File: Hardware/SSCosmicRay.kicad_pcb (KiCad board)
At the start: 2 copper layers, 80 x 50 mm, 115 parts, among them J1 ICSP-PIC, J2 USB_MINI, SW1 PGM, SW2 RST, U1 MAX4477, U2 MAX4477, U3 MAX991, U4 741G08, U5 PIC32MX250F128B, U6 MAX4477, U7 MAX4477, U8 LTC3129-SOP, U9 AOZ1280, X1 8MHz

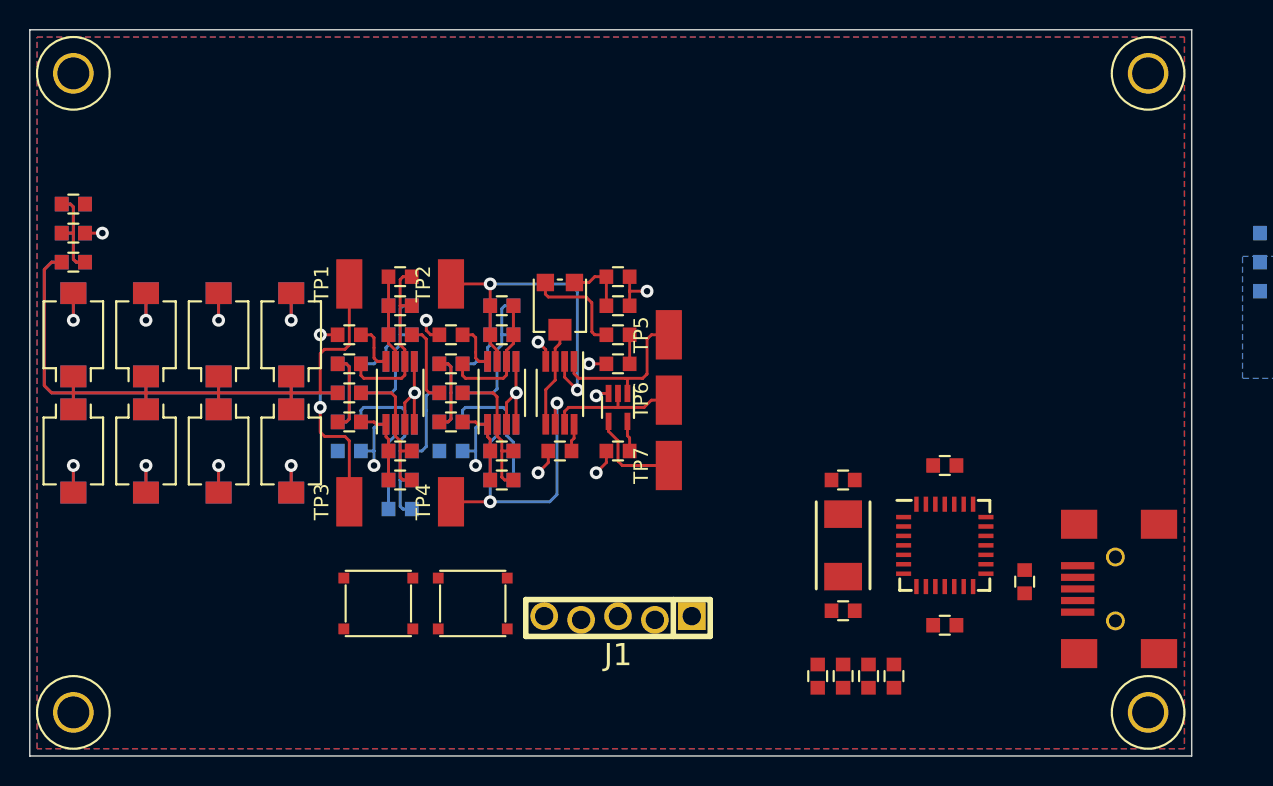
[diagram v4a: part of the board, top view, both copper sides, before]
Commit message: Switch to 44 pin PIC
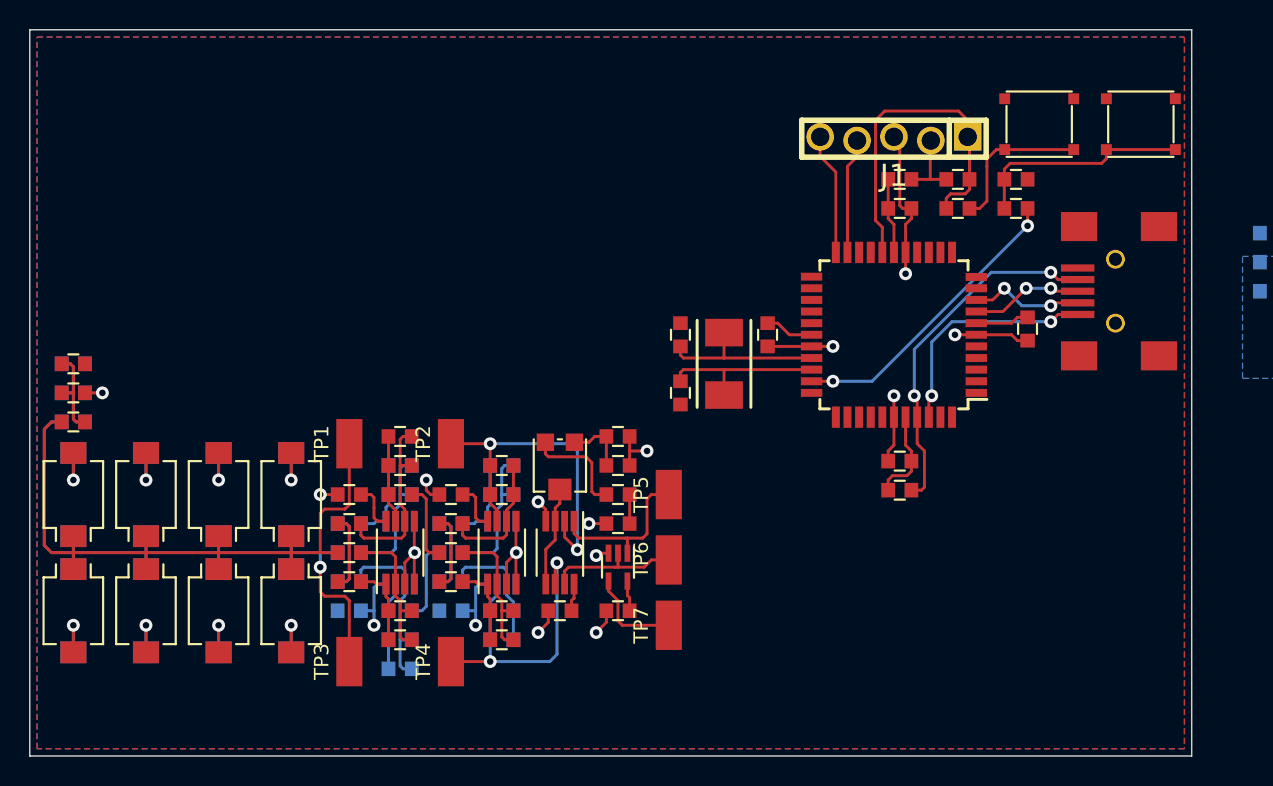
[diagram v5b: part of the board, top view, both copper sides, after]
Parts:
- removed MECH-HOLE220 (x4): VAL**, MECH-HOLE220
- added C41: 0.1uF, CAPC1608-N, F.Cu at (186.9, 65.3)
- added R31: 10k, RESC1608-N, F.Cu at (186.9, 84.7)
- added R32: 10, RESC1608-N, F.Cu at (186.9, 63.3)
- R15: value R -> 10k
- U5: value PIC32MX250F128B -> PIC32MX250F128D; footprint QFN65P600X600-28N -> QFP80P1200x1200-44N
- moved SW1 62.0 mm to (203.5, 59.5), turned to 180 degrees
- moved SW2 51.1 mm to (196.5, 59.5), turned to 180 degrees
- moved J1 38.1 mm to (186.5, 60.5)
- moved R13 36.2 mm to (194.9, 63.3), turned to 180 degrees
- moved R12 35.0 mm to (194.9, 65.3), turned to 180 degrees
- moved R14 34.5 mm to (190.9, 63.3), turned to 0 degrees
- moved R15 32.8 mm to (190.9, 65.3), turned to 0 degrees
- moved J2 20.5 mm to (207.0, 71.0)
- moved C17 18.7 mm to (171.8, 78.0), turned to 270 degrees
- moved C18 17.4 mm to (195.7, 73.6)
- moved C19 15.2 mm to (177.8, 74.0), turned to 270 degrees
- moved C16 15.0 mm to (171.8, 74.0), turned to 90 degrees
- moved X1 14.9 mm to (174.8, 76.0)
- moved U5 14.9 mm to (186.5, 74.0), turned to 180 degrees
- moved C20 11.7 mm to (186.9, 82.7), turned to 180 degrees
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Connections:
- U5 pad 1: /Processor/PGD -> (no net)
- U5 pad 11: /Processor/ID -> (no net)
- U5 pad 12: /Processor/VBus -> (no net)
- U5 pad 17: /Processor/VCap -> /Processor/VAng
- U5 pad 18: /Processor/D+ -> /Processor/MCLR
- U5 pad 19: /Processor/D- -> (no net)
- U5 pad 2: /Processor/PGC -> (no net)
- U5 pad 20: +3.3V -> (no net)
- U5 pad 21: (no net) -> /Processor/PGD
- U5 pad 22: (no net) -> /Processor/PGC
- U5 pad 23: (no net) -> /Processor/A1
- U5 pad 24: GND -> /Processor/A2
- U5 pad 25: +3.3V -> /Processor/C1
- U5 pad 26: /Processor/MCLR -> /Processor/C2
- U5 pad 27: (no net) -> /Processor/C
- U5 pad 28: (no net) -> +3.3V
- U5 pad 5: GND -> (no net)
- U5 pad 6: /Processor/OSC1 -> GND
- U5 pad 7: /Processor/OSC2 -> /Processor/VCap
- U5 pad 8: /Processor/PGM -> /Processor/D+
- U5 pad 9: (no net) -> /Processor/D-
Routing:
- net GND: track 71.5 -> 96.3 mm, vias 25 -> 29
- net /Processor/ID: track 0.00 -> 24.4 mm, vias 0 -> 2
- net /Processor/MCLR: track 0.00 -> 23.5 mm
- net /Processor/PGM: track 0.00 -> 20.5 mm, vias 0 -> 2
- net /Processor/VBus: track 0.00 -> 16.1 mm, vias 0 -> 2
- net N-0000028: track 0.00 -> 15.4 mm
- net +3.3V: track 21.5 -> 36.4 mm
- net /Processor/OSC2: track 0.00 -> 11.5 mm
- net /Processor/OSC1: track 0.00 -> 11.5 mm
- net N-0000027: track 0.00 -> 10.6 mm
- net /Processor/PGC: track 0.00 -> 8.40 mm
- net /Processor/PGD: track 0.00 -> 7.98 mm
- net /Processor/D-: track 0.00 -> 7.89 mm, vias 0 -> 2
- net /Processor/D+: track 0.00 -> 7.73 mm, vias 0 -> 2
- net /Processor/VAng: track 0.00 -> 5.20 mm
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
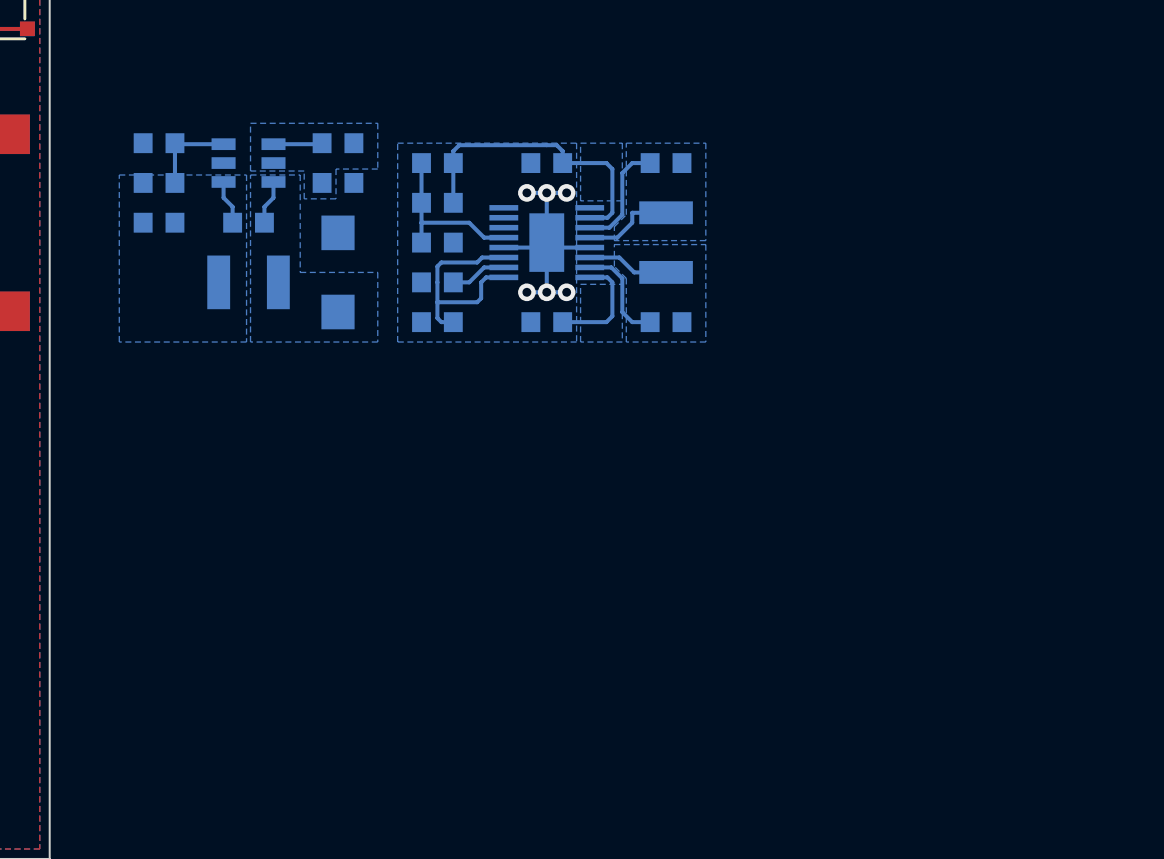
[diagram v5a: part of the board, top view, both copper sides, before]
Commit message: Change bias supply to reference layout
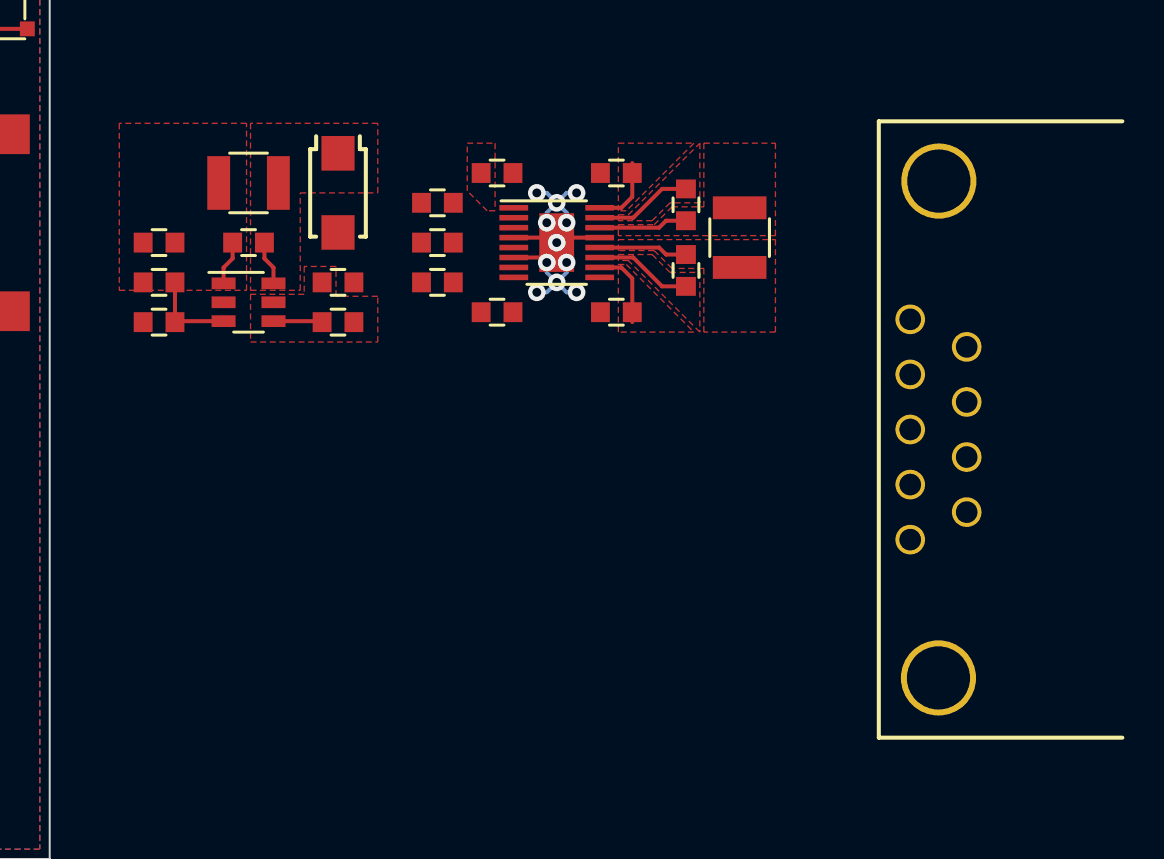
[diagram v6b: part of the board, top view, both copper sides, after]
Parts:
- added J3: CONN-9, CONN-TE-1734354, F.Cu at (261.2, 81.4)
- C32, C33, C34, C35, C36, C37, C38, C39, C40, D17, L1, L2, R25, R26, R27, R28, R29, R30, U8, U9: moved to F.Cu
- moved R27 9.00 mm to (221.5, 76.0)
- moved R29 9.00 mm to (212.5, 76.0)
- moved C34 8.28 mm to (235.5, 68.5)
- moved C36 8.28 mm to (235.5, 75.5)
- moved C35 8.08 mm to (229.5, 75.5)
- moved C37 8.08 mm to (229.5, 68.5), turned to 0 degrees
- moved U9 7.00 mm to (217.0, 75.0), turned to 270 degrees
- moved C32 5.98 mm to (239.0, 70.1), turned to 90 degrees
- moved C33 5.49 mm to (239.0, 73.4), turned to 270 degrees
- moved C40 5.00 mm to (221.5, 74.0)
- moved L2 5.00 mm to (217.0, 69.0)
- moved R28 5.00 mm to (212.5, 74.0)
- moved D17 4.00 mm to (221.5, 69.5), turned to 270 degrees
- moved R25 4.00 mm to (226.5, 74.0)
- moved R30 4.00 mm to (226.5, 70.0)
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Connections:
- C37 pad 1: N-0000082 (its old number) -> /Power/Vcc
- U5 pad 1: (no net) -> /Processor/SDA/DO
- U5 pad 44: (no net) -> /Processor/SCL/DI
- U8 pad 1: N-0000082 (its old number) -> /Power/Vcc
- U8 pad 3: N-0000082 (its old number) -> /Power/Vcc
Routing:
- net GND: track 96.3 -> 109.1 mm, vias 29 -> 34
- net N-0000082 (its old number): track 11.3 -> 0.00 mm
- net +12V: track 15.0 -> 4.07 mm
- net N-0000084: track 8.45 -> 0.00 mm
- net N-0000081: track 2.85 -> 0.00 mm
- net VCOM: track 5.57 -> 3.57 mm
- net /Power/BS2: track 5.62 -> 4.94 mm
- added copper zone on F.Cu, net +12V
- added copper zone on F.Cu, net /Power/BS1
- added copper zone on F.Cu, net /Power/BS2
- added copper zone on F.Cu, net /Power/Lx
- added copper zone on F.Cu, net /Power/SW1
- added copper zone on F.Cu, net /Power/SW2
- added copper zone on F.Cu, net /Power/Vcc
- added copper zone on F.Cu, net VCOM
- removed copper zone on B.Cu, net +12V
- removed copper zone on B.Cu, net +3.3V
- removed copper zone on B.Cu, net /Power/Lx
- removed copper zone on B.Cu, net /Power/SW1
- removed copper zone on B.Cu, net /Power/SW2
- removed copper zone on B.Cu, net VCOM

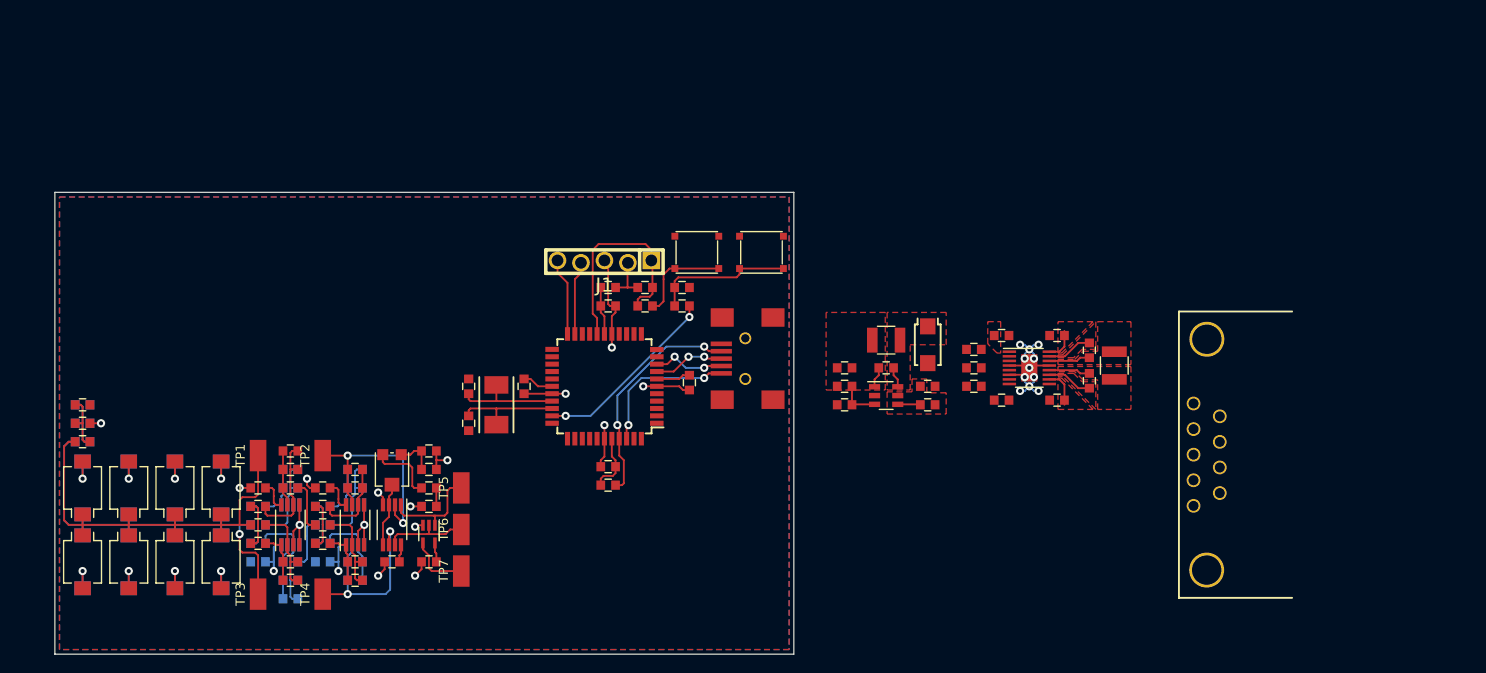
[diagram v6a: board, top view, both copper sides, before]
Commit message: Change to vertical USB port
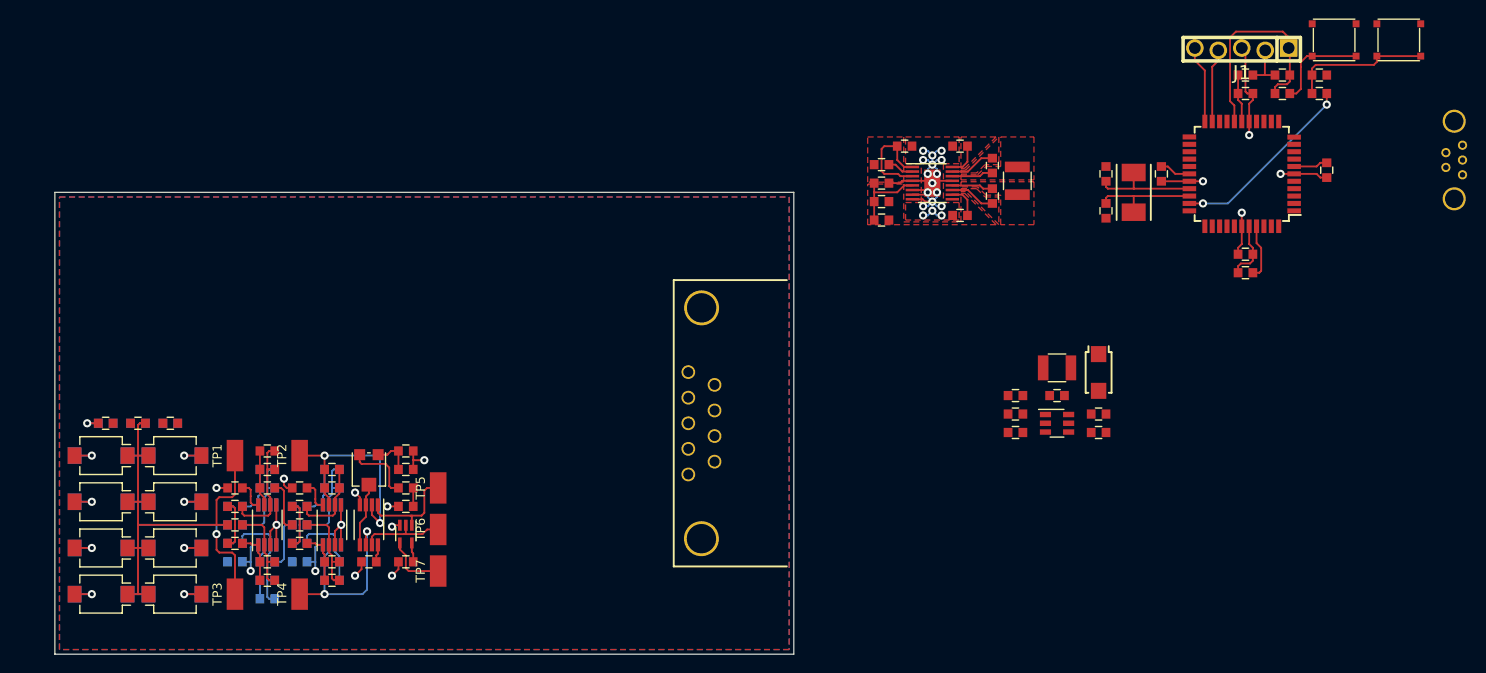
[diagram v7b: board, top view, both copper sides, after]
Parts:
- J2: footprint CONN-USB-M26FTR -> CONN-WURTH-651005136421; moved to B.Cu
- moved J2 74.7 mm to (278.5, 49.5), turned to 270 degrees
- moved C16 72.7 mm to (240.8, 51.0)
- moved C17 72.7 mm to (240.8, 55.0)
- moved C19 72.7 mm to (246.8, 51.0)
- moved C20 72.7 mm to (255.9, 59.7)
- moved C41 72.7 mm to (255.9, 42.3)
- moved J1 72.7 mm to (255.5, 37.5)
- moved R31 72.7 mm to (255.9, 61.7)
- moved R32 72.7 mm to (255.9, 40.3)
- moved SW1 72.7 mm to (272.5, 36.5)
- moved SW2 72.7 mm to (265.5, 36.5)
- moved U5 72.7 mm to (255.5, 51.0)
- moved X1 72.7 mm to (243.8, 53.0)
- moved C18 72.7 mm to (264.7, 50.6)
- moved R12 72.7 mm to (263.9, 42.3)
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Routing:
- net /Processor/ID: track 24.4 -> 6.02 mm, vias 2 -> 0
- net /Processor/VBus: track 16.1 -> 0.00 mm, vias 2 -> 0
- net GND: track 109.1 -> 123.4 mm, vias 34 -> 40
- net /Power/Vcc: track 0.00 -> 11.2 mm
- net N-0000084: track 0.00 -> 8.45 mm
- net /Processor/D-: track 7.89 -> 0.00 mm, vias 2 -> 0
- net /Processor/D+: track 7.73 -> 0.00 mm, vias 2 -> 0
- net N-0000075: track 6.17 -> 0.00 mm
- net N-0000010: track 6.17 -> 0.00 mm
- net N-0000078: track 4.47 -> 0.00 mm
- net N-0000081: track 0.00 -> 2.85 mm
- net N-0000082: track 2.47 -> 0.00 mm
- net N-0000076: track 2.24 -> 0.00 mm
- net /Power/Lx: track 2.24 -> 0.00 mm
- net /Amplifier 2/In: track 48.0 -> 47.1 mm
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- added copper zone on F.Cu, net GND
- removed copper zone on F.Cu, net /Power/Lx
